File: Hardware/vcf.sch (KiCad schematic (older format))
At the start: 63 parts, among them U1 TL074, U2 TL074, U3 TL074

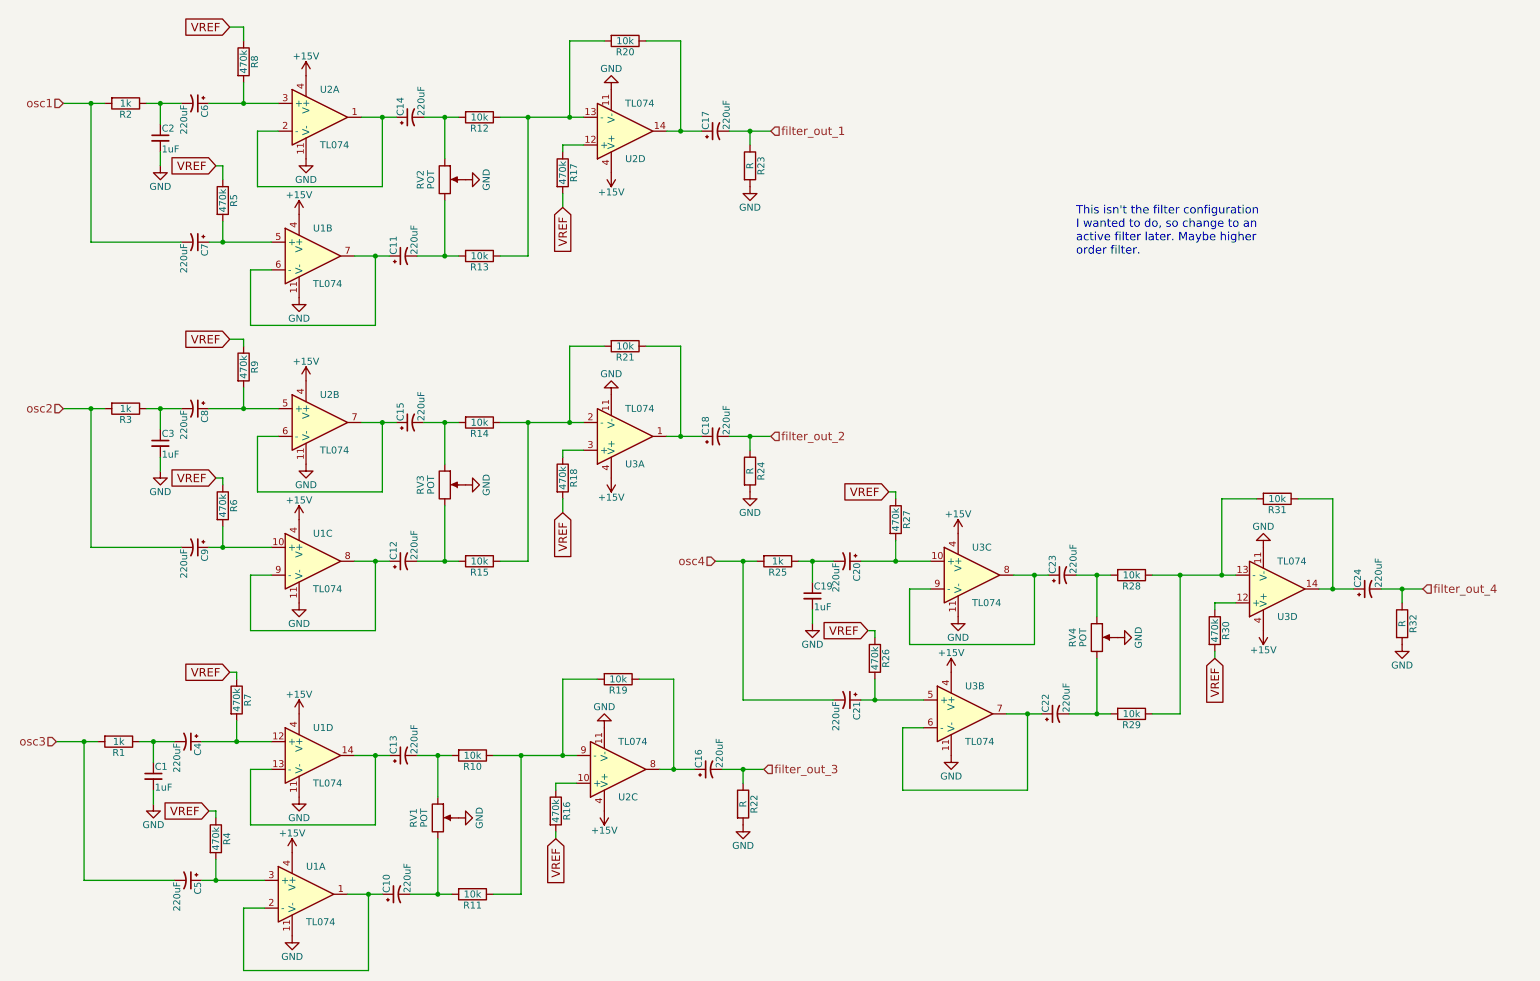
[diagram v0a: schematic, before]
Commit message: add analog LFO to schematic
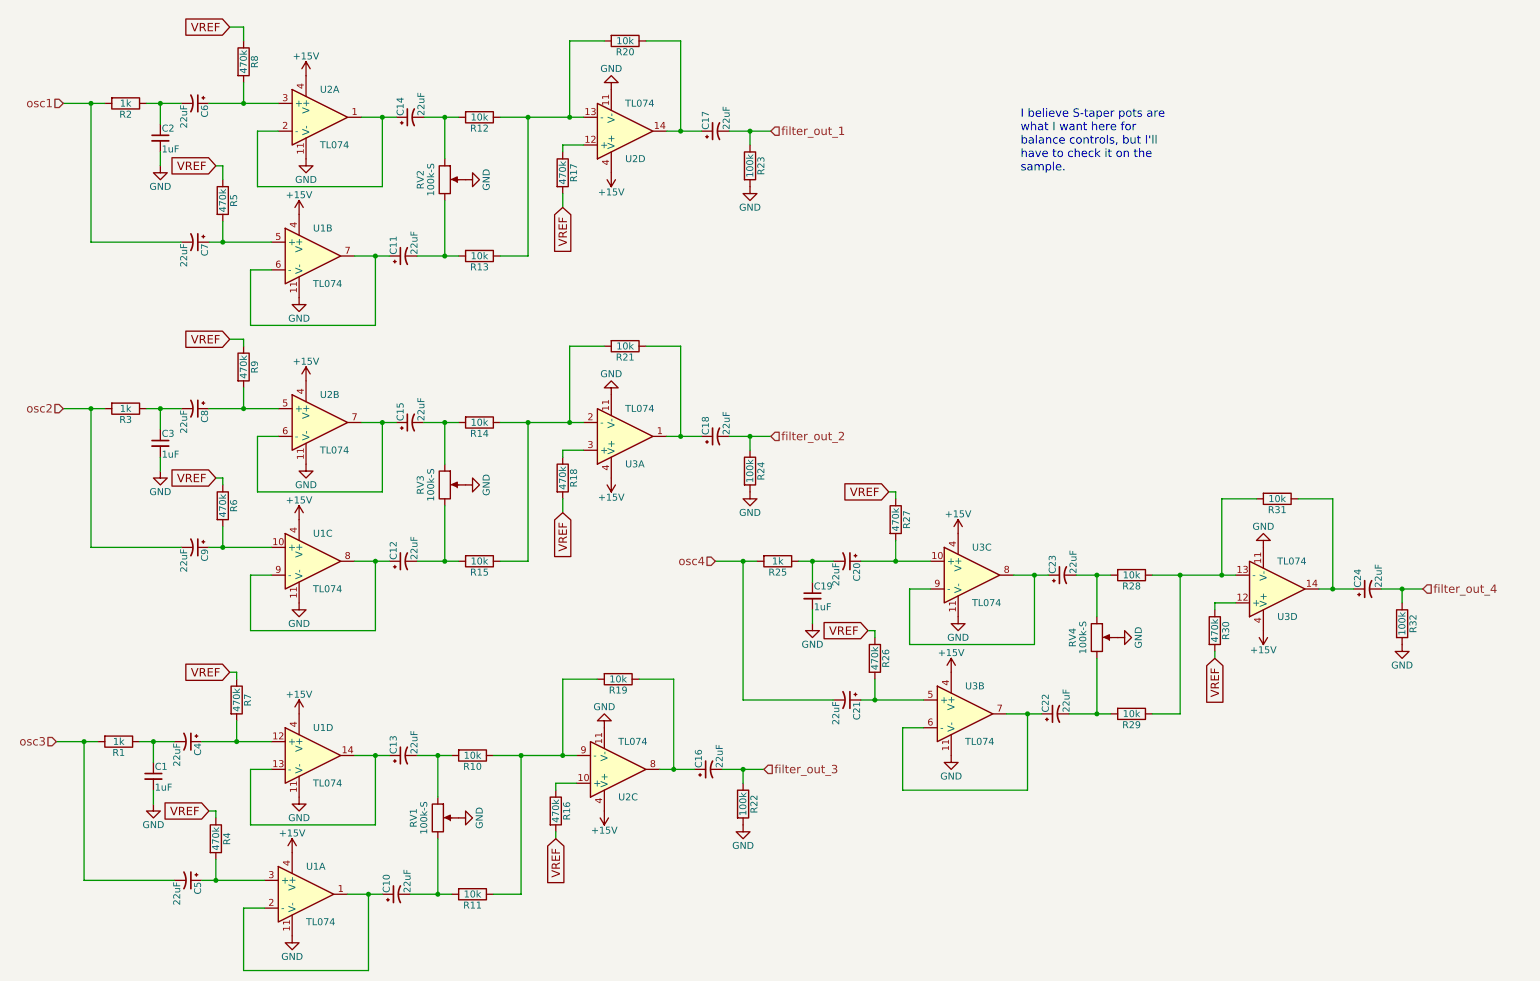
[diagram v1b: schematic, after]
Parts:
- C10, C11, C12, C13, C14, C15, C16, C17, C18, C20, C21, C22, C23, C24, C4, C5, C6, C7, C8, C9: value 220uF -> 22uF
- R22, R23, R24, R32: value R -> 100k
- RV1, RV2, RV3, RV4: value POT -> 100k-S
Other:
- note added: "I believe S-taper pots are \nwhat I want here for \nbalance controls, but I'll \nhave to check it on the \nsample."
- note removed: "This isn't the filter configuration \nI wanted to do, so change to an \nactive filter later. Maybe higher \norder filter."
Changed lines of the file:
@@
 P 1750 1100
 F 0 "C6" H 1760 1170 50  0000 L CNN
-F 1 "220uF" H 1760 1020 50  0000 L CNN
+F 1 "22uF" H 1760 1020 50  0000 L CNN
 F 2 "" H 1750 1100 50  0001 C CNN
 F 3 "" H 1750 1100 50  0001 C CNN
@@
 P 3300 1200
 F 0 "C14" H 3310 1270 50  0000 L CNN
-F 1 "220uF" H 3310 1120 50  0000 L CNN
+F 1 "22uF" H 3310 1120 50  0000 L CNN
 F 2 "" H 3300 1200 50  0001 C CNN
 F 3 "" H 3300 1200 50  0001 C CNN
@@
 P 1750 2100
 F 0 "C7" H 1760 2170 50  0000 L CNN
-F 1 "220uF" H 1760 2020 50  0000 L CNN
+F 1 "22uF" H 1760 2020 50  0000 L CNN
 F 2 "" H 1750 2100 50  0001 C CNN
 F 3 "" H 1750 2100 50  0001 C CNN
@@
 P 3250 2200
 F 0 "C11" H 3260 2270 50  0000 L CNN
-F 1 "220uF" H 3260 2120 50  0000 L CNN
+F 1 "22uF" H 3260 2120 50  0000 L CNN
 F 2 "" H 3250 2200 50  0001 C CNN
 F 3 "" H 3250 2200 50  0001 C CNN
@@
 P 3550 1650
 F 0 "RV2" V 3375 1650 50  0000 C CNN
-F 1 "POT" V 3450 1650 50  0000 C CNN
+F 1 "100k-S" V 3450 1650 50  0000 C CNN
 F 2 "" H 3550 1650 50  0001 C CNN
 F 3 "" H 3550 1650 50  0001 C CNN
@@
 P 5500 1300
 F 0 "C17" H 5510 1370 50  0000 L CNN
-F 1 "220uF" H 5510 1220 50  0000 L CNN
+F 1 "22uF" H 5510 1220 50  0000 L CNN
 F 2 "" H 5500 1300 50  0001 C CNN
 F 3 "" H 5500 1300 50  0001 C CNN
@@
 P 5750 1550
 F 0 "R23" V 5830 1550 50  0000 C CNN
-F 1 "R" V 5750 1550 50  0000 C CNN
+F 1 "100k" V 5750 1550 50  0000 C CNN
 F 2 "" V 5680 1550 50  0001 C CNN
 F 3 "" H 5750 1550 50  0001 C CNN
@@
 P 1750 3300
 F 0 "C8" H 1760 3370 50  0000 L CNN
-F 1 "220uF" H 1760 3220 50  0000 L CNN
+F 1 "22uF" H 1760 3220 50  0000 L CNN
 F 2 "" H 1750 3300 50  0001 C CNN
 F 3 "" H 1750 3300 50  0001 C CNN
@@
 P 3300 3400
 F 0 "C15" H 3310 3470 50  0000 L CNN
-F 1 "220uF" H 3310 3320 50  0000 L CNN
+F 1 "22uF" H 3310 3320 50  0000 L CNN
 F 2 "" H 3300 3400 50  0001 C CNN
 F 3 "" H 3300 3400 50  0001 C CNN
@@
 P 1750 4300
 F 0 "C9" H 1760 4370 50  0000 L CNN
-F 1 "220uF" H 1760 4220 50  0000 L CNN
+F 1 "22uF" H 1760 4220 50  0000 L CNN
 F 2 "" H 1750 4300 50  0001 C CNN
 F 3 "" H 1750 4300 50  0001 C CNN
@@
 P 3250 4400
 F 0 "C12" H 3260 4470 50  0000 L CNN
-F 1 "220uF" H 3260 4320 50  0000 L CNN
+F 1 "22uF" H 3260 4320 50  0000 L CNN
 F 2 "" H 3250 4400 50  0001 C CNN
 F 3 "" H 3250 4400 50  0001 C CNN
@@
 P 3550 3850
 F 0 "RV3" V 3375 3850 50  0000 C CNN
-F 1 "POT" V 3450 3850 50  0000 C CNN
+F 1 "100k-S" V 3450 3850 50  0000 C CNN
 F 2 "" H 3550 3850 50  0001 C CNN
 F 3 "" H 3550 3850 50  0001 C CNN
@@
 P 5500 3500
 F 0 "C18" H 5510 3570 50  0000 L CNN
-F 1 "220uF" H 5510 3420 50  0000 L CNN
+F 1 "22uF" H 5510 3420 50  0000 L CNN
 F 2 "" H 5500 3500 50  0001 C CNN
 F 3 "" H 5500 3500 50  0001 C CNN
@@
 P 5750 3750
 F 0 "R24" V 5830 3750 50  0000 C CNN
-F 1 "R" V 5750 3750 50  0000 C CNN
+F 1 "100k" V 5750 3750 50  0000 C CNN
 F 2 "" V 5680 3750 50  0001 C CNN
 F 3 "" H 5750 3750 50  0001 C CNN
@@
 P 1700 5700
 F 0 "C4" H 1710 5770 50  0000 L CNN
-F 1 "220uF" H 1710 5620 50  0000 L CNN
+F 1 "22uF" H 1710 5620 50  0000 L CNN
 F 2 "" H 1700 5700 50  0001 C CNN
 F 3 "" H 1700 5700 50  0001 C CNN
@@
 P 3250 5800
 F 0 "C13" H 3260 5870 50  0000 L CNN
-F 1 "220uF" H 3260 5720 50  0000 L CNN
+F 1 "22uF" H 3260 5720 50  0000 L CNN
 F 2 "" H 3250 5800 50  0001 C CNN
 F 3 "" H 3250 5800 50  0001 C CNN
@@
 P 1700 6700
 F 0 "C5" H 1710 6770 50  0000 L CNN
-F 1 "220uF" H 1710 6620 50  0000 L CNN
+F 1 "22uF" H 1710 6620 50  0000 L CNN
 F 2 "" H 1700 6700 50  0001 C CNN
 F 3 "" H 1700 6700 50  0001 C CNN
@@
 P 3200 6800
 F 0 "C10" H 3210 6870 50  0000 L CNN
-F 1 "220uF" H 3210 6720 50  0000 L CNN
+F 1 "22uF" H 3210 6720 50  0000 L CNN
 F 2 "" H 3200 6800 50  0001 C CNN
 F 3 "" H 3200 6800 50  0001 C CNN
@@
 P 3500 6250
 F 0 "RV1" V 3325 6250 50  0000 C CNN
-F 1 "POT" V 3400 6250 50  0000 C CNN
+F 1 "100k-S" V 3400 6250 50  0000 C CNN
 F 2 "" H 3500 6250 50  0001 C CNN
 F 3 "" H 3500 6250 50  0001 C CNN
@@
 P 5450 5900
 F 0 "C16" H 5460 5970 50  0000 L CNN
-F 1 "220uF" H 5460 5820 50  0000 L CNN
+F 1 "22uF" H 5460 5820 50  0000 L CNN
 F 2 "" H 5450 5900 50  0001 C CNN
 F 3 "" H 5450 5900 50  0001 C CNN
@@
 P 5700 6150
 F 0 "R22" V 5780 6150 50  0000 C CNN
-F 1 "R" V 5700 6150 50  0000 C CNN
+F 1 "100k" V 5700 6150 50  0000 C CNN
 F 2 "" V 5630 6150 50  0001 C CNN
 F 3 "" H 5700 6150 50  0001 C CNN
@@
 P 6450 4400
 F 0 "C20" H 6460 4470 50  0000 L CNN
-F 1 "220uF" H 6460 4320 50  0000 L CNN
+F 1 "22uF" H 6460 4320 50  0000 L CNN
 F 2 "" H 6450 4400 50  0001 C CNN
 F 3 "" H 6450 4400 50  0001 C CNN
@@
 P 8000 4500
 F 0 "C23" H 8010 4570 50  0000 L CNN
-F 1 "220uF" H 8010 4420 50  0000 L CNN
+F 1 "22uF" H 8010 4420 50  0000 L CNN
 F 2 "" H 8000 4500 50  0001 C CNN
 F 3 "" H 8000 4500 50  0001 C CNN
@@
 P 6450 5400
 F 0 "C21" H 6460 5470 50  0000 L CNN
-F 1 "220uF" H 6460 5320 50  0000 L CNN
+F 1 "22uF" H 6460 5320 50  0000 L CNN
 F 2 "" H 6450 5400 50  0001 C CNN
 F 3 "" H 6450 5400 50  0001 C CNN
@@
 P 7950 5500
 F 0 "C22" H 7960 5570 50  0000 L CNN
-F 1 "220uF" H 7960 5420 50  0000 L CNN
+F 1 "22uF" H 7960 5420 50  0000 L CNN
 F 2 "" H 7950 5500 50  0001 C CNN
 F 3 "" H 7950 5500 50  0001 C CNN
@@
 P 8250 4950
 F 0 "RV4" V 8075 4950 50  0000 C CNN
-F 1 "POT" V 8150 4950 50  0000 C CNN
+F 1 "100k-S" V 8150 4950 50  0000 C CNN
 F 2 "" H 8250 4950 50  0001 C CNN
 F 3 "" H 8250 4950 50  0001 C CNN
@@
 P 10200 4600
 F 0 "C24" H 10210 4670 50  0000 L CNN
-F 1 "220uF" H 10210 4520 50  0000 L CNN
+F 1 "22uF" H 10210 4520 50  0000 L CNN
 F 2 "" H 10200 4600 50  0001 C CNN
 F 3 "" H 10200 4600 50  0001 C CNN
@@
 P 10450 4850
 F 0 "R32" V 10530 4850 50  0000 C CNN
-F 1 "R" V 10450 4850 50  0000 C CNN
+F 1 "100k" V 10450 4850 50  0000 C CNN
 F 2 "" V 10380 4850 50  0001 C CNN
 F 3 "" H 10450 4850 50  0001 C CNN
@@
 	-1   0    0    1
 $EndComp
-Text Notes 8100 2200 0    60   ~ 0
-This isn't the filter configuration \nI wanted to do, so change to an \nactive filter later. Maybe higher \norder filter.
 Text GLabel 2000 550  0    60   Input ~ 0
 VREF
@@
 Wire Wire Line
 	9100 5100 9100 5050
+Text Notes 7700 1600 0    60   ~ 0
+I believe S-taper pots are \nwhat I want here for \nbalance controls, but I'll \nhave to check it on the \nsample.
 $EndSCHEMATC

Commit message: associate footprints with all components
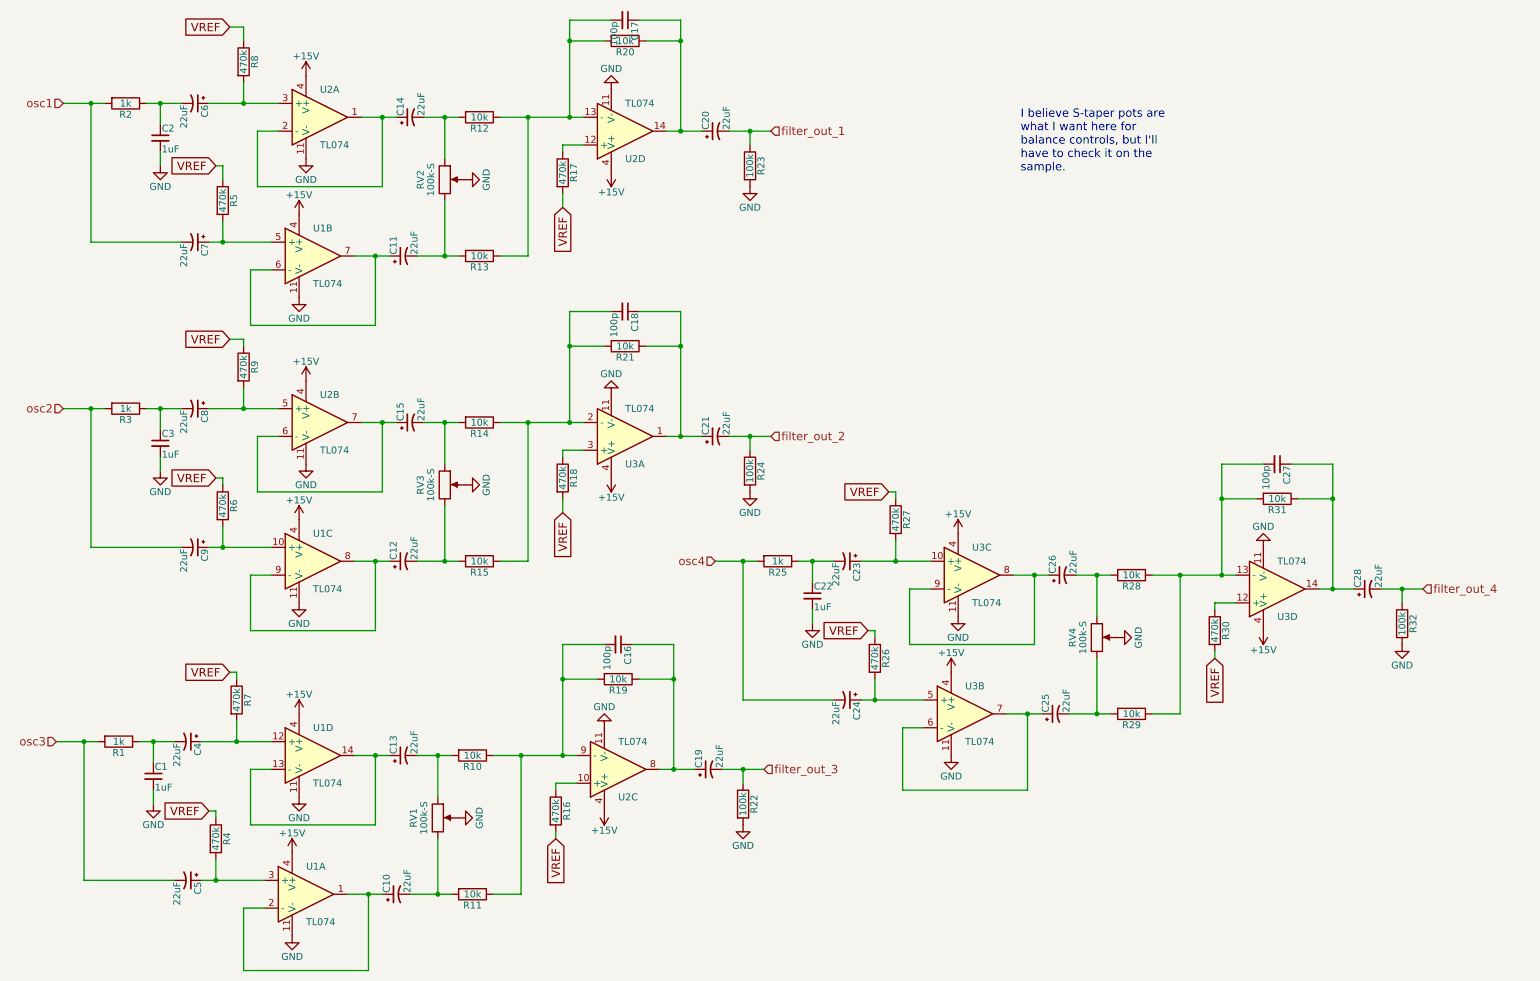
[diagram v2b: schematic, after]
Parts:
- added C16, C17, C18, C27: 100p, digikey-footprints:0805, symbol C_Small
- C1, C2, C3: footprint (none) -> Capacitors_SMD:CP_Elec_4x4.5
- C10, C11, C12, C13, C14, C15, C4, C5, C6, C7, C8, C9: footprint (none) -> Capacitors_SMD:CP_Elec_5x5.7
- C19: renamed from C16; footprint (none) -> Capacitors_SMD:CP_Elec_5x5.7
- C20: renamed from C17; footprint (none) -> Capacitors_SMD:CP_Elec_5x5.7
- C21: renamed from C18; footprint (none) -> Capacitors_SMD:CP_Elec_5x5.7
- C22: renamed from C19; footprint (none) -> Capacitors_SMD:CP_Elec_4x4.5
- C23: renamed from C20; footprint (none) -> Capacitors_SMD:CP_Elec_5x5.7
- C24: renamed from C21; footprint (none) -> Capacitors_SMD:CP_Elec_5x5.7
- C25: renamed from C22; footprint (none) -> Capacitors_SMD:CP_Elec_5x5.7
- C26: renamed from C23; footprint (none) -> Capacitors_SMD:CP_Elec_5x5.7
- C28: renamed from C24; footprint (none) -> Capacitors_SMD:CP_Elec_5x5.7
- R1, R10, R11, R12, R13, R14, R15, R16, R17, R18, R19, R2, R20, R21, R22, R23, R24, R25, R26, R27, R28, R29, R3, R30, R31, R32, R4, R5, R6, R7, R8, R9: footprint (none) -> digikey-footprints:0805
- RV1, RV2, RV3, RV4: footprint (none) -> Potentiometers:Potentiometer_Bourns_PTV09A-1_Horizontal
- U1, U2, U3: footprint (none) -> digikey-footprints:SOIC-14_W3.9mm
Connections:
- net at R12.1, R13.1, R20.2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: now also C17.2
- net at C20.1, R20.1, U2.14: now also C17.1
- net at R14.1, R15.1, R21.2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: now also C18.2
- net at C21.1, R21.1, U3.1: now also C18.1
- net at R10.1, R11.1, R19.2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: now also C16.2
- net at C19.1, R19.1, U2.8: now also C16.1
- net at R28.1, R29.1, R31.2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: now also C27.2
- net at C28.1, R31.1, U3.14: now also C27.1
